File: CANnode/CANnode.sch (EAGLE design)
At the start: 247 parts, among them IC1 ISO1050DUB, IC2 ISO1050DUB, Q1 FDV302P, Q3 FDV302P, U1 LM324PW, U10 FT2232HL, U11 93LC56C-I/SN, U2 TPS70445_PWP_24, U3 LM324PW, U4 LM324PW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

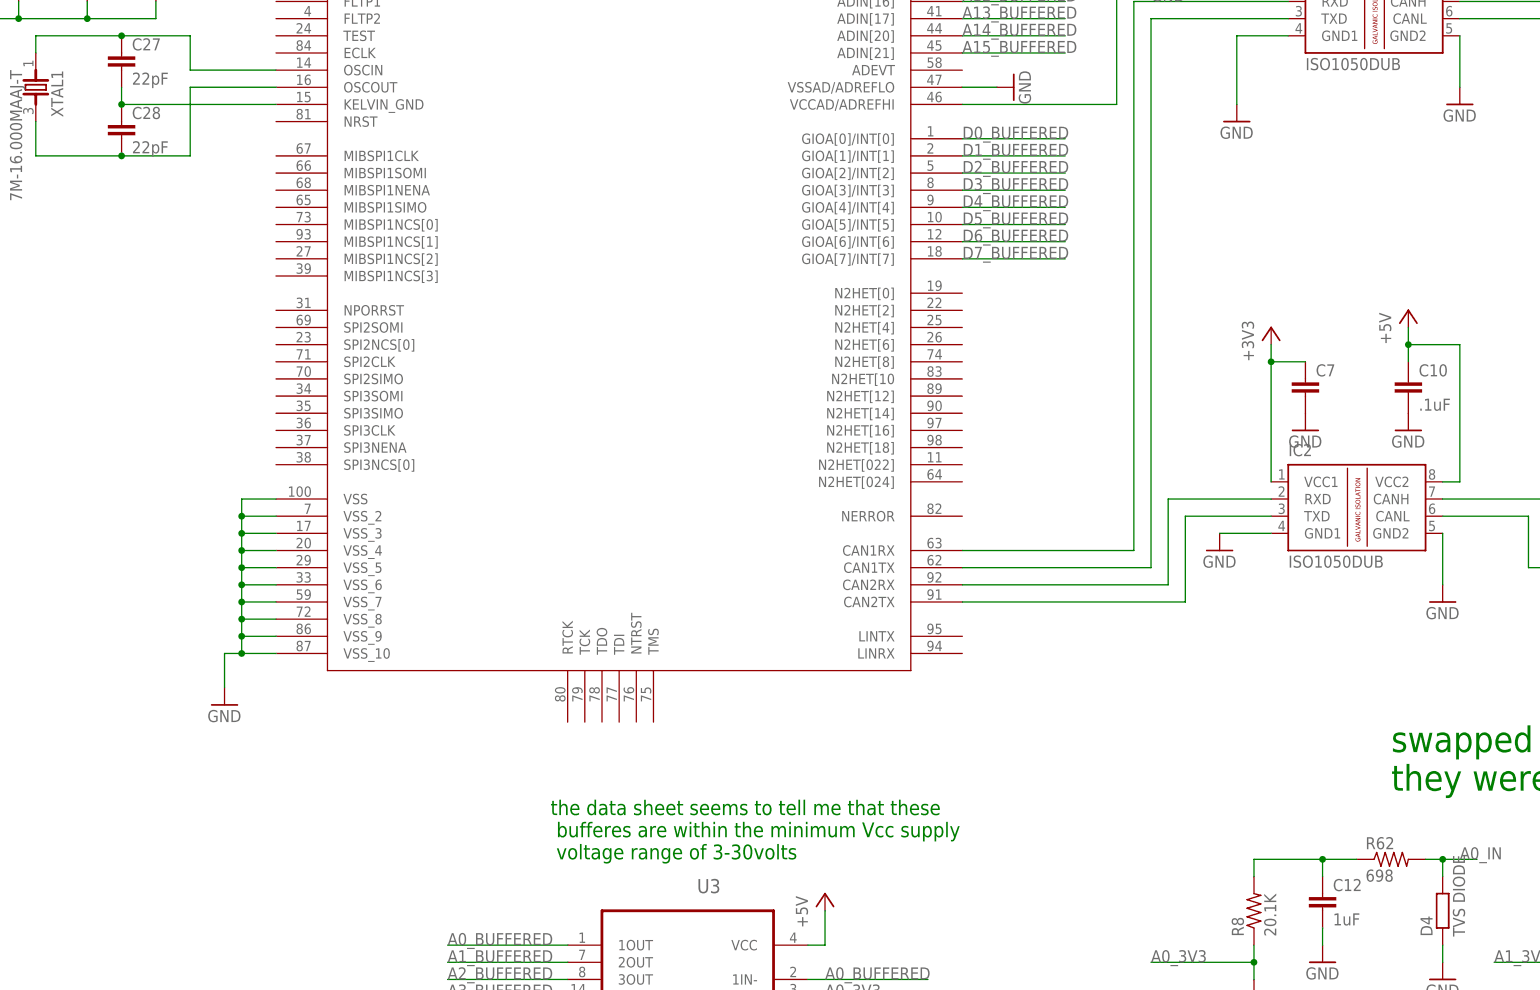
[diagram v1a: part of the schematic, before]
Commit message: Added missing JTAG connection to MCU
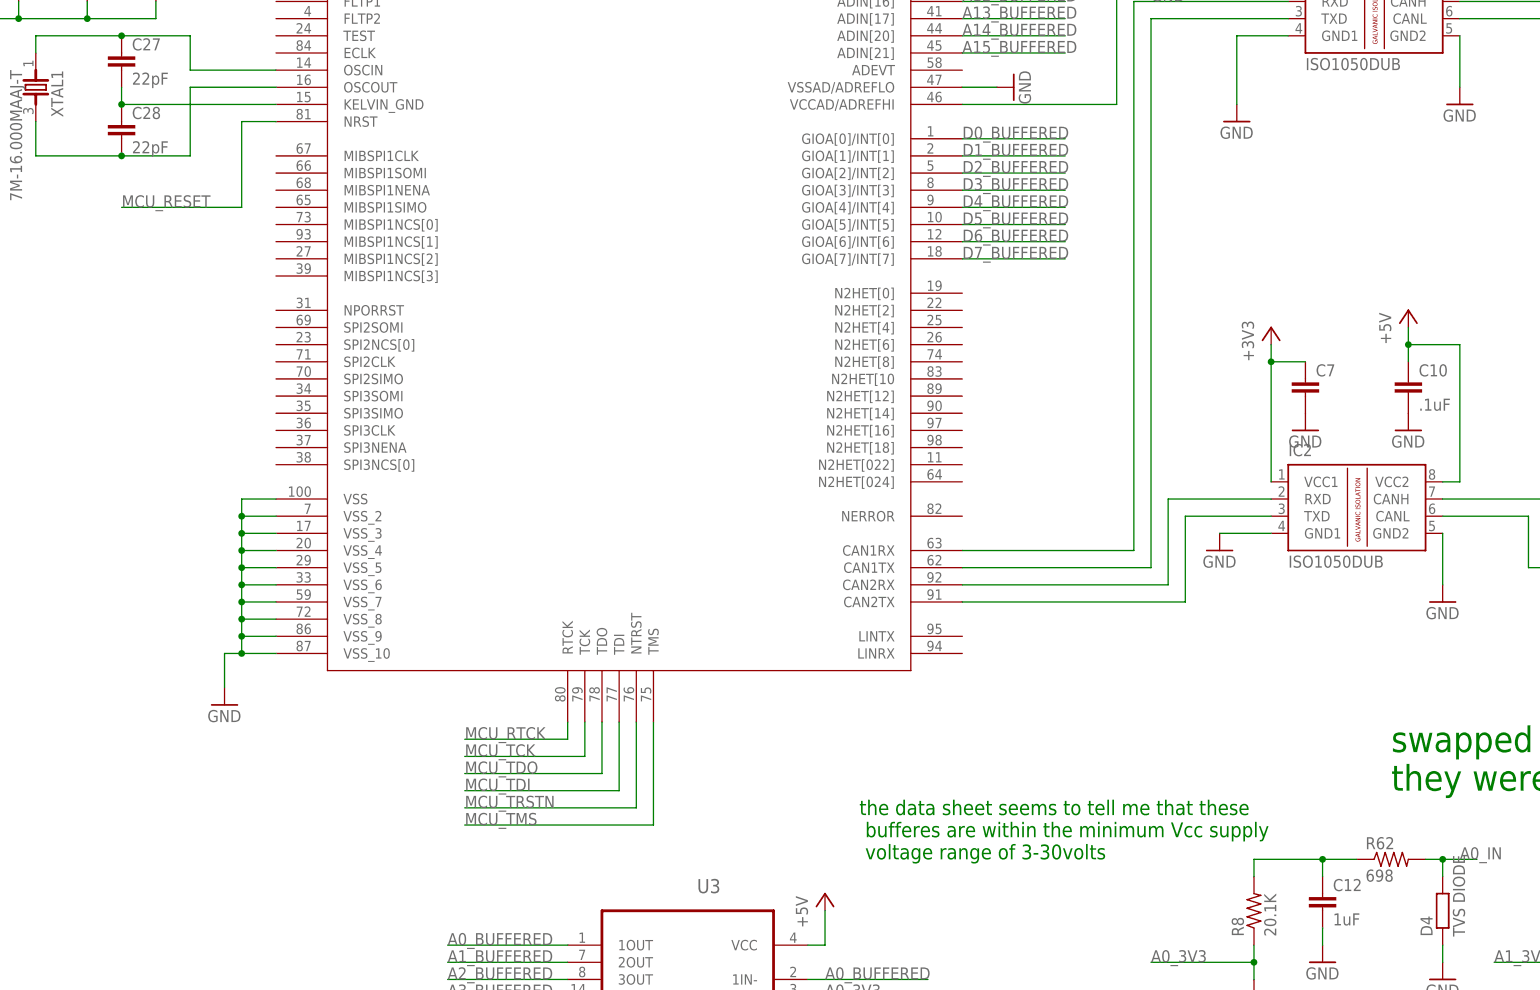
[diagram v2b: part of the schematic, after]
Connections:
- net MCU_RESET: now also U7.NRST
- net MCU_RTCK: now also U7.RTCK
- net MCU_TCK: now also U7.TCK
- net MCU_TDI: now also U7.TDI
- net MCU_TDO: now also U7.TDO
- net MCU_TMS: now also U7.TMS
- net MCU_TRSTN: now also U7.NTRST
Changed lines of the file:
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@@
 <?xml version="1.0" encoding="utf-8"?>
 <!DOCTYPE eagle SYSTEM "eagle.dtd">
-<eagle version="7.5.0">
+<eagle version="6.6.0">
 <drawing>
 <settings>
@@
 <text x="495.3" y="-86.36" size="3.81" layer="91">swapped all of the resisters in the input stages.
 they were the wrong values</text>
-<text x="370.84" y="-96.52" size="2.1844" layer="91">the data sheet seems to tell me that these
+<text x="416.56" y="-96.52" size="2.1844" layer="91">the data sheet seems to tell me that these
  bufferes are within the minimum Vcc supply
  voltage range of 3-30volts</text>
@@
 <pinref part="R86" gate="G$1" pin="2"/>
 </segment>
+<segment>
+<pinref part="U7" gate="A" pin="RTCK"/>
+<wire x1="373.38" y1="-76.2" x2="373.38" y2="-78.74" width="0.1524" layer="91"/>
+<wire x1="373.38" y1="-78.74" x2="358.14" y2="-78.74" width="0.1524" layer="91"/>
+<label x="358.14" y="-78.74" size="1.778" layer="95"/>
+</segment>
 </net>
 <net name="SUSPEED" class="0">
@@
 <pinref part="R95" gate="G$1" pin="1"/>
 </segment>
+<segment>
+<pinref part="U7" gate="A" pin="TMS"/>
+<wire x1="386.08" y1="-76.2" x2="386.08" y2="-91.44" width="0.1524" layer="91"/>
+<wire x1="386.08" y1="-91.44" x2="358.14" y2="-91.44" width="0.1524" layer="91"/>
+<label x="358.14" y="-91.44" size="1.778" layer="95"/>
+</segment>
 </net>
 <net name="MCU_TRSTN" class="0">
@@
 <pinref part="R94" gate="G$1" pin="1"/>
 </segment>
+<segment>
+<pinref part="U7" gate="A" pin="NTRST"/>
+<wire x1="383.54" y1="-76.2" x2="383.54" y2="-88.9" width="0.1524" layer="91"/>
+<wire x1="383.54" y1="-88.9" x2="358.14" y2="-88.9" width="0.1524" layer="91"/>
+<label x="358.14" y="-88.9" size="1.778" layer="95"/>
+</segment>
 </net>
 <net name="MCU_TDI" class="0">
@@
 <pinref part="R93" gate="G$1" pin="1"/>
 </segment>
+<segment>
+<pinref part="U7" gate="A" pin="TDI"/>
+<wire x1="381" y1="-76.2" x2="381" y2="-86.36" width="0.1524" layer="91"/>
+<wire x1="381" y1="-86.36" x2="358.14" y2="-86.36" width="0.1524" layer="91"/>
+<label x="358.14" y="-86.36" size="1.778" layer="95"/>
+</segment>
 </net>
 <net name="T_DIS" class="0">
@@
 <pinref part="R91" gate="G$1" pin="1"/>
 </segment>
+<segment>
+<pinref part="U7" gate="A" pin="TDO"/>
+<wire x1="378.46" y1="-76.2" x2="378.46" y2="-83.82" width="0.1524" layer="91"/>
+<wire x1="378.46" y1="-83.82" x2="358.14" y2="-83.82" width="0.1524" layer="91"/>
+<label x="358.14" y="-83.82" size="1.778" layer="95"/>
+</segment>
 </net>
 <net name="MCU_TCK" class="0">
@@
 <pinref part="R90" gate="G$1" pin="1"/>
 </segment>
+<segment>
+<pinref part="U7" gate="A" pin="TCK"/>
+<wire x1="375.92" y1="-76.2" x2="375.92" y2="-81.28" width="0.1524" layer="91"/>
+<wire x1="375.92" y1="-81.28" x2="358.14" y2="-81.28" width="0.1524" layer="91"/>
+<label x="358.14" y="-81.28" size="1.778" layer="95"/>
+</segment>
 </net>
 <net name="MCU_RESET" class="0">
@@
 <pinref part="R89" gate="G$1" pin="1"/>
 </segment>
+<segment>
+<pinref part="U7" gate="A" pin="NRST"/>
+<wire x1="330.2" y1="12.7" x2="325.12" y2="12.7" width="0.1524" layer="91"/>
+<wire x1="325.12" y1="12.7" x2="325.12" y2="0" width="0.1524" layer="91"/>
+<wire x1="325.12" y1="0" x2="307.34" y2="0" width="0.1524" layer="91"/>
+<label x="307.34" y="0" size="1.778" layer="95"/>
+</segment>
 </net>

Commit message: added comment to move TVS after resistor on USB input
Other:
- note added: "move TVS to after resistor to limit current"
- note removed: "DM and DP are data lines. we need to wither pass them though a JTAG debugging chip, or somehow dont do that and get them to the proper data ports."
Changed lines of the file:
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@@
  is VCC_SRAM, and VNMA?</text>
 <text x="71.12" y="-38.1" size="1.778" layer="91">made a test point</text>
-<text x="22.86" y="-73.66" size="1.778" layer="91">DM and DP are data lines. we need to wither pass
- them though a JTAG debugging chip, or somehow
- dont do that and get them to the proper data ports.</text>
+<text x="22.86" y="-73.66" size="1.778" layer="91">move TVS to after resistor to limit current</text>
 <text x="20.32" y="-109.22" size="3.81" layer="91">THESE ARE PLACEHOLDER RESISTERS THAT WE WILL
 SWITCH WITH THE TVS's IN THE LATER STAGES!!!!! </text>

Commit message: Added PTC fuse
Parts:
- F1: value (none) -> 0ZCJ0050AF2E; device special:FUSE -> adafruit:PTCFUSE-1206
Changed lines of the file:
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@@
 <layers>
 <layer number="1" name="Top" color="4" fill="1" visible="no" active="no"/>
+<layer number="2" name="Route2" color="1" fill="3" visible="no" active="no"/>
+<layer number="15" name="Route15" color="4" fill="6" visible="no" active="no"/>
 <layer number="16" name="Bottom" color="1" fill="1" visible="no" active="no"/>
 <layer number="17" name="Pads" color="2" fill="1" visible="no" active="no"/>
@@
 <layer number="54" name="bGND_GNDA" color="7" fill="1" visible="no" active="no"/>
 <layer number="56" name="wert" color="7" fill="1" visible="no" active="no"/>
+<layer number="57" name="tCAD" color="7" fill="1" visible="no" active="no"/>
 <layer number="59" name="tCarbon" color="7" fill="1" visible="no" active="no"/>
 <layer number="60" name="bCarbon" color="7" fill="1" visible="no" active="no"/>
@@
 <layer number="111" name="LPC17xx" color="7" fill="1" visible="yes" active="yes"/>
 <layer number="112" name="tSilk" color="7" fill="1" visible="yes" active="yes"/>
+<layer number="113" name="ReferenceLS" color="7" fill="1" visible="no" active="no"/>
 <layer number="116" name="Patch_BOT" color="7" fill="1" visible="no" active="yes"/>
+<layer number="118" name="Rect_Pads" color="7" fill="1" visible="no" active="no"/>
 <layer number="121" name="_tsilk" color="7" fill="1" visible="no" active="yes"/>
 <layer number="122" name="_bsilk" color="7" fill="1" visible="no" active="yes"/>
@@
 <layer number="132" name="bAdjust" color="7" fill="1" visible="no" active="yes"/>
 <layer number="144" name="Drill_legend" color="7" fill="1" visible="yes" active="yes"/>
+<layer number="150" name="Notes" color="7" fill="1" visible="no" active="yes"/>
 <layer number="151" name="HeatSink" color="7" fill="1" visible="no" active="yes"/>
 <layer number="152" name="_bDocu" color="7" fill="1" visible="yes" active="yes"/>
+<layer number="153" name="FabDoc1" color="6" fill="1" visible="no" active="no"/>
+<layer number="154" name="FabDoc2" color="2" fill="1" visible="no" active="no"/>
+<layer number="155" name="FabDoc3" color="7" fill="15" visible="no" active="no"/>
 <layer number="199" name="Contour" color="7" fill="1" visible="yes" active="yes"/>
 <layer number="200" name="200bmp" color="1" fill="10" visible="no" active="no"/>
@@
 <layer number="223" name="223bmp" color="24" fill="1" visible="yes" active="yes"/>
 <layer number="224" name="224bmp" color="25" fill="1" visible="yes" active="yes"/>
+<layer number="225" name="225bmp" color="7" fill="1" visible="yes" active="yes"/>
+<layer number="226" name="226bmp" color="7" fill="1" visible="yes" active="yes"/>
+<layer number="227" name="227bmp" color="7" fill="1" visible="yes" active="yes"/>
+<layer number="228" name="228bmp" color="7" fill="1" visible="yes" active="yes"/>
+<layer number="229" name="229bmp" color="7" fill="1" visible="yes" active="yes"/>
+<layer number="230" name="230bmp" color="7" fill="1" visible="yes" active="yes"/>
+<layer number="231" name="Eagle3D_PG1" color="7" fill="1" visible="no" active="no"/>
+<layer number="232" name="Eagle3D_PG2" color="7" fill="1" visible="no" active="no"/>
+<layer number="233" name="Eagle3D_PG3" color="7" fill="1" visible="no" active="no"/>
 <layer number="248" name="Housing" color="7" fill="1" visible="yes" active="yes"/>
 <layer number="249" name="Edge" color="7" fill="1" visible="yes" active="yes"/>
@@
 <layer number="251" name="SMDround" color="12" fill="11" visible="no" active="no"/>
 <layer number="254" name="cooling" color="7" fill="1" visible="no" active="yes"/>
+<layer number="255" name="routoute" color="7" fill="1" visible="yes" active="yes"/>
 </layers>
 <schematic xreflabel="%F%N/%S.%C%R" xrefpart="/%S.%C%R">
@@
 <part name="U$1" library="supply1" deviceset="+1V2" device=""/>
 <part name="R3" library="resistor" deviceset="R-US_" device="R0402" value="499k"/>
-<part name="F1" library="special" deviceset="FUSE" device=""/>
 <part name="LED1" library="led" deviceset="LED" device=""/>
 <part name="R4" library="varistor" deviceset="VARISTOR" device="CN0805"/>
@@
 <part name="C74" library="eagle-ltspice" deviceset="C" device="C0402" value="100nF"/>
 <part name="GND123" library="supply1" deviceset="GND" device=""/>
+<part name="F1" library="adafruit" deviceset="PTCFUSE" device="-1206" value="0ZCJ0050AF2E"/>
 </parts>
 <sheets>
@@
 <instance part="U$1" gate="A" x="248.92" y="2.54"/>
 <instance part="R3" gate="G$1" x="30.48" y="5.08" rot="R90"/>
-<instance part="F1" gate="G$1" x="15.24" y="12.7"/>
 <instance part="LED1" gate="G$1" x="30.48" y="-5.08"/>
 <instance part="R4" gate="G$1" x="0" y="5.08" rot="R90"/>
@@
 <instance part="C74" gate="G$1" x="58.42" y="5.08"/>
 <instance part="GND123" gate="1" x="58.42" y="-5.08"/>
+<instance part="F1" gate="G$1" x="15.24" y="10.16"/>
 </instances>
 <busses>
@@
 </segment>
 <segment>
-<pinref part="F1" gate="G$1" pin="1"/>
-<wire x1="7.62" y1="12.7" x2="0" y2="12.7" width="0.1524" layer="91"/>
+<wire x1="10.16" y1="12.7" x2="0" y2="12.7" width="0.1524" layer="91"/>
 <pinref part="R4" gate="G$1" pin="1"/>
 <wire x1="0" y1="10.16" x2="0" y2="12.7" width="0.1524" layer="91"/>
@@
 <wire x1="0" y1="12.7" x2="-15.24" y2="12.7" width="0.1524" layer="91"/>
 <label x="-15.24" y="12.7" size="1.778" layer="95"/>
+<pinref part="F1" gate="G$1" pin="1"/>
 </segment>
 <segment>
@@
 <junction x="68.58" y="12.7"/>
 <wire x1="68.58" y1="12.7" x2="58.42" y2="12.7" width="0.1524" layer="91"/>
-<pinref part="F1" gate="G$1" pin="2"/>
 <pinref part="R3" gate="G$1" pin="2"/>
 <wire x1="58.42" y1="12.7" x2="50.8" y2="12.7" width="0.1524" layer="91"/>
@@
 <wire x1="58.42" y1="7.62" x2="58.42" y2="12.7" width="0.1524" layer="91"/>
 <junction x="58.42" y="12.7"/>
+<pinref part="F1" gate="G$1" pin="2"/>
 </segment>
 <segment>

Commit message: Connected JTAG to RM42. Board size reduced to 2.17x2.28. Relocated power supply components
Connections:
- removed net CHIP_RESET: U2.*EN1, U2.*EN2, U2.GND/HEATSINK, U2.GND/HEATSINK_2, U2.GND/HEATSINK_3, U2.GND/HEATSINK_4, U2.GND/HEATSINK_5
- net GND: now also U2.*EN1, U2.*EN2, U2.GND/HEATSINK, U2.GND/HEATSINK_2, U2.GND/HEATSINK_3, U2.GND/HEATSINK_4, U2.GND/HEATSINK_5
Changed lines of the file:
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@@
 <?xml version="1.0" encoding="utf-8"?>
 <!DOCTYPE eagle SYSTEM "eagle.dtd">
-<eagle version="6.6.0">
+<eagle version="7.5.0">
 <drawing>
 <settings>
@@
 </busses>
 <nets>
-<net name="CHIP_RESET" class="0">
-<segment>
-<pinref part="U2" gate="A" pin="GND/HEATSINK_2"/>
-<wire x1="104.14" y1="17.78" x2="93.98" y2="17.78" width="0.1524" layer="91"/>
-</segment>
-<segment>
-<wire x1="104.14" y1="-2.54" x2="93.98" y2="-2.54" width="0.1524" layer="91"/>
-<pinref part="U2" gate="A" pin="GND/HEATSINK_3"/>
-<pinref part="U2" gate="A" pin="*EN1"/>
-<wire x1="104.14" y1="5.08" x2="93.98" y2="5.08" width="0.1524" layer="91"/>
-<wire x1="93.98" y1="5.08" x2="93.98" y2="2.54" width="0.1524" layer="91"/>
-<pinref part="U2" gate="A" pin="*EN2"/>
-<wire x1="93.98" y1="2.54" x2="93.98" y2="-2.54" width="0.1524" layer="91"/>
-<wire x1="104.14" y1="2.54" x2="93.98" y2="2.54" width="0.1524" layer="91"/>
-<junction x="93.98" y="2.54"/>
-<junction x="93.98" y="5.08"/>
-<junction x="93.98" y="-2.54"/>
-</segment>
-<segment>
-<wire x1="104.14" y1="-10.16" x2="93.98" y2="-10.16" width="0.1524" layer="91"/>
-<pinref part="U2" gate="A" pin="GND/HEATSINK_4"/>
-</segment>
-<segment>
-<wire x1="210.82" y1="15.24" x2="200.66" y2="15.24" width="0.1524" layer="91"/>
-<pinref part="U2" gate="A" pin="GND/HEATSINK"/>
-</segment>
-<segment>
-<wire x1="210.82" y1="-12.7" x2="200.66" y2="-12.7" width="0.1524" layer="91"/>
-<pinref part="U2" gate="A" pin="GND/HEATSINK_5"/>
-</segment>
-</net>
 <net name="N$1" class="0">
 <segment>
@@
 <wire x1="58.42" y1="-2.54" x2="58.42" y2="0" width="0.1524" layer="91"/>
 </segment>
+<segment>
+<pinref part="U2" gate="A" pin="GND/HEATSINK_2"/>
+<wire x1="104.14" y1="17.78" x2="93.98" y2="17.78" width="0.1524" layer="91"/>
+</segment>
+<segment>
+<wire x1="210.82" y1="15.24" x2="200.66" y2="15.24" width="0.1524" layer="91"/>
+<pinref part="U2" gate="A" pin="GND/HEATSINK"/>
+</segment>
+<segment>
+<wire x1="104.14" y1="-2.54" x2="93.98" y2="-2.54" width="0.1524" layer="91"/>
+<pinref part="U2" gate="A" pin="GND/HEATSINK_3"/>
+<pinref part="U2" gate="A" pin="*EN1"/>
+<wire x1="104.14" y1="5.08" x2="93.98" y2="5.08" width="0.1524" layer="91"/>
+<wire x1="93.98" y1="5.08" x2="93.98" y2="2.54" width="0.1524" layer="91"/>
+<pinref part="U2" gate="A" pin="*EN2"/>
+<wire x1="93.98" y1="2.54" x2="93.98" y2="-2.54" width="0.1524" layer="91"/>
+<wire x1="104.14" y1="2.54" x2="93.98" y2="2.54" width="0.1524" layer="91"/>
+<junction x="93.98" y="2.54"/>
+<junction x="93.98" y="5.08"/>
+<junction x="93.98" y="-2.54"/>
+</segment>
+<segment>
+<wire x1="104.14" y1="-10.16" x2="93.98" y2="-10.16" width="0.1524" layer="91"/>
+<pinref part="U2" gate="A" pin="GND/HEATSINK_4"/>
+</segment>
+<segment>
+<wire x1="210.82" y1="-12.7" x2="200.66" y2="-12.7" width="0.1524" layer="91"/>
+<pinref part="U2" gate="A" pin="GND/HEATSINK_5"/>
+</segment>
 </net>
